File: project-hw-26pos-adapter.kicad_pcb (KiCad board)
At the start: 2 copper layers, 38 x 52 mm, 3 parts, among them J1 SM04B-SRSS-TB(LF)(SN), J2 3220-26-0300-00, U1 Pink Panda v2.1.0

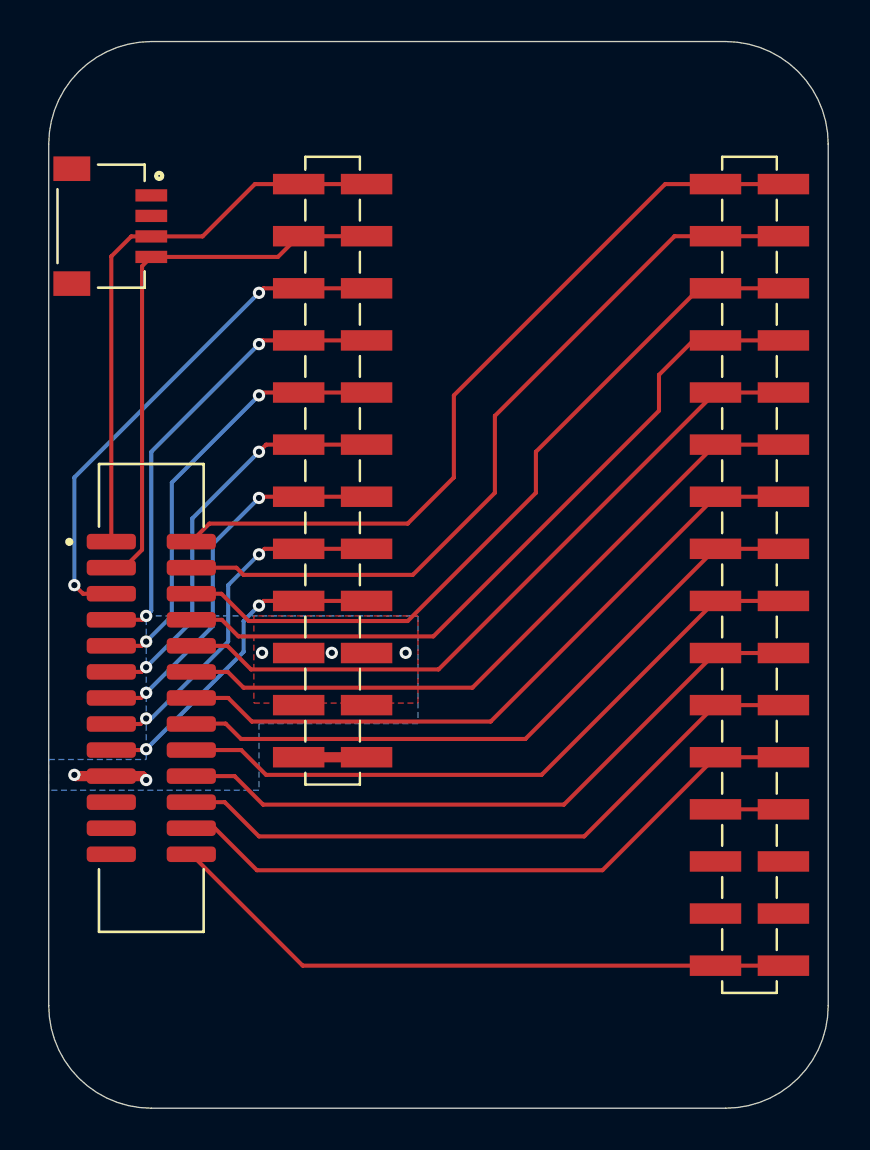
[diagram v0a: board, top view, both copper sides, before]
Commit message: pcb: complete routing
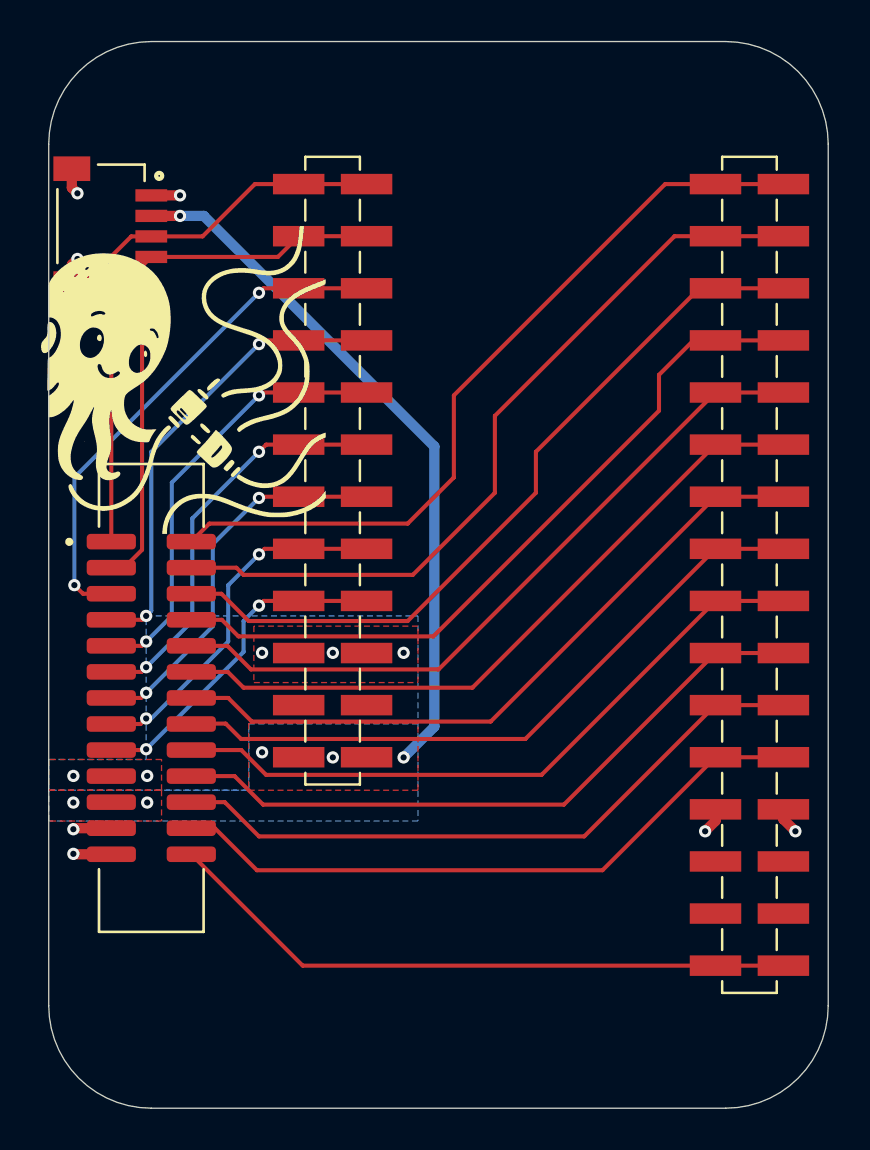
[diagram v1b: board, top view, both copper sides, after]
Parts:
- added G***: LOGO, logos:octopus_15mm, F.Cu at (38.0, 35.5)
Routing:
- net /VDD_OUT: track 3.31 -> 34.2 mm, vias 0 -> 6
- net GND: track 3.31 -> 10.3 mm, vias 0 -> 7
- net /USB: track 3.60 -> 0.00 mm
- added copper zone on B.Cu, net /VDD_OUT
- added copper zone on F.Cu, net /VDD_OUT
- added copper zone on In1.Cu, net GND
- added copper zone on In2.Cu, net GND
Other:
- copper layers 2 -> 4

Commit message: Print 1:1
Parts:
- moved G*** 0.25 mm to (38.2, 35.5)
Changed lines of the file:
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@@
 	(footprint "logos:octopus_15mm"
 		(layer "F.Cu")
-		(at 38 35.5)
+		(at 38.25 35.5)
 		(property "Reference" "G***"
 			(at 0 0 0)

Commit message: pcb: add version on board
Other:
- board text added: "v1.0.0"
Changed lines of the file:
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@@
 		(layer "Edge.Cuts")
+	)
+	(gr_text "v1.0.0"
+		(at 68 68 0)
+		(layer "B.SilkS")
+		(effects
+			(font
+				(face "FreeSans")
+				(size 1.5 1.5)
+				(thickness 0.1)
+			)
+			(justify left bottom mirror)
+		)
+		(render_cache "v1.0.0" 0
+			(polygon
+				(pts
+					(xy 67.398429 67.745) (xy 67.590771 67.745) (xy 67.97875 66.642976) (xy 67.780547 66.642976) (xy 67.485258 67.536905)
+					(xy 67.172749 66.642976) (xy 66.974546 66.642976)
+				)
+			)
+			(polygon
+				(pts
+					(xy 66.412909 66.666423) (xy 66.744103 66.666423) (xy 66.744103 66.525739) (xy 66.668712 66.515289)
+					(xy 66.594039 66.501339) (xy 66.519052 66.480622) (xy 66.463468 66.453932) (xy 66.413026 66.397253)
+					(xy 66.378093 66.327158) (xy 66.352568 66.254492) (xy 66.349528 66.244371) (xy 66.227163 66.244371)
+					(xy 66.227163 67.745) (xy 66.412909 67.745)
+				)
+			)
+			(polygon
+				(pts
+					(xy 65.404675 67.533974) (xy 65.404675 67.745) (xy 65.624127 67.745) (xy 65.624127 67.533974)
+				)
+			)
+			(polygon
+				(pts
+					(xy 64.747572 66.247597) (xy 64.819958 66.261224) (xy 64.88758 66.288643) (xy 64.949651 66.328635)
+					(xy 64.97026 66.345072) (xy 65.023114 66.399087) (xy 65.065788 66.459794) (xy 65.068794 66.464892)
+					(xy 65.10236 66.53556) (xy 65.126789 66.607831) (xy 65.146022 66.683276) (xy 65.149837 66.701308)
+					(xy 65.162637 66.77687) (xy 65.171498 66.857929) (xy 65.176021 66.933362) (xy 65.177529 67.013004)
+					(xy 65.177408 67.03664) (xy 65.174488 67.127627) (xy 65.167676 67.212924) (xy 65.156971 67.292531)
+					(xy 65.142374 67.366448) (xy 65.118653 67.450842) (xy 65.08885 67.526346) (xy 65.052965 67.592958)
+					(xy 65.036943 67.617048) (xy 64.983448 67.679993) (xy 64.921813 67.72895) (xy 64.852037 67.763919)
+					(xy 64.774122 67.7849) (xy 64.688066 67.791894) (xy 64.658696 67.791126) (xy 64.57589 67.779598)
+					(xy 64.501045 67.754237) (xy 64.434159 67.715043) (xy 64.375233 67.662017) (xy 64.324267 67.595157)
+					(xy 64.316536 67.582666) (xy 64.281561 67.515073) (xy 64.252722 67.438911) (xy 64.23002 67.35418)
+					(xy 64.216275 67.280226) (xy 64.206458 67.200788) (xy 64.200567 67.115866) (xy 64.198604 67.02546)
+					(xy 64.198945 67.008607) (xy 64.388381 67.008607) (xy 64.389537 67.085246) (xy 64.394234 67.173767)
+					(xy 64.402546 67.254203) (xy 64.41447 67.326553) (xy 64.43355 67.402699) (xy 64.462386 67.476821)
+					(xy 64.492912 67.528118) (xy 64.549616 67.585163) (xy 64.619419 67.618329) (xy 64.692463 67.627763)
+					(xy 64.777532 67.612799) (xy 64.848182 67.567907) (xy 64.894321 67.510445) (xy 64.931232 67.433829)
+					(xy 64.95286 67.363797) (xy 64.969297 67.282991) (xy 64.980543 67.191411) (xy 64.986599 67.089057)
+					(xy 64.987752 67.014836) (xy 64.98746 66.977532) (xy 64.98307 66.872726) (xy 64.973412 66.778579)
+					(xy 64.958486 66.69509) (xy 64.930391 66.60035) (xy 64.89293 66.524559) (xy 64.846104 66.467715)
+					(xy 64.774402 66.423306) (xy 64.688066 66.408503) (xy 64.651776 66.410847) (xy 64.571294 66.437219)
+					(xy 64.505445 66.492892) (xy 64.463302 66.558529) (xy 64.430524 66.642919) (xy 64.412086 66.718518)
+					(xy 64.398916 66.804665) (xy 64.391014 66.901362) (xy 64.388381 67.008607) (xy 64.198945 67.008607)
+					(xy 64.200516 66.930875) (xy 64.206252 66.842392) (xy 64.215811 66.760012) (xy 64.229195 66.683734)
+					(xy 64.256441 66.580758) (xy 64.29229 66.491513) (xy 64.336743 66.415997) (xy 64.3898 66.354212)
+					(xy 64.451461 66.306157) (xy 64.521726 66.271832) (xy 64.600594 66.251236) (xy 64.688066 66.244371)
+				)
+			)
+			(polygon
+				(pts
+					(xy 63.713538 67.533974) (xy 63.713538 67.745) (xy 63.93299 67.745) (xy 63.93299 67.533974)
+				)
+			)
+			(polygon
+				(pts
+					(xy 63.056435 66.247597) (xy 63.12882 66.261224) (xy 63.196442 66.288643) (xy 63.258513 66.328635)
+					(xy 63.279123 66.345072) (xy 63.331977 66.399087) (xy 63.374651 66.459794) (xy 63.377657 66.464892)
+					(xy 63.411222 66.53556) (xy 63.435651 66.607831) (xy 63.454884 66.683276) (xy 63.4587 66.701308)
+					(xy 63.4715 66.77687) (xy 63.480361 66.857929) (xy 63.484884 66.933362) (xy 63.486392 67.013004)
+					(xy 63.48627 67.03664) (xy 63.483351 67.127627) (xy 63.476538 67.212924) (xy 63.465834 67.292531)
+					(xy 63.451236 67.366448) (xy 63.427516 67.450842) (xy 63.397713 67.526346) (xy 63.361828 67.592958)
+					(xy 63.345805 67.617048) (xy 63.29231 67.679993) (xy 63.230675 67.72895) (xy 63.1609 67.763919)
+					(xy 63.082985 67.7849) (xy 62.996929 67.791894) (xy 62.967558 67.791126) (xy 62.884753 67.779598)
+					(xy 62.809907 67.754237) (xy 62.743021 67.715043) (xy 62.684095 67.662017) (xy 62.633129 67.595157)
+					(xy 62.625398 67.582666) (xy 62.590424 67.515073) (xy 62.561585 67.438911) (xy 62.538882 67.35418)
+					(xy 62.525138 67.280226) (xy 62.51532 67.200788) (xy 62.50943 67.115866) (xy 62.507466 67.02546)
+					(xy 62.507807 67.008607) (xy 62.697243 67.008607) (xy 62.698399 67.085246) (xy 62.703097 67.173767)
+					(xy 62.711408 67.254203) (xy 62.723333 67.326553) (xy 62.742412 67.402699) (xy 62.771249 67.476821)
+					(xy 62.801774 67.528118) (xy 62.858478 67.585163) (xy 62.928282 67.618329) (xy 63.001325 67.627763)
+					(xy 63.086394 67.612799) (xy 63.157045 67.567907) (xy 63.203184 67.510445) (xy 63.240095 67.433829)
+					(xy 63.261722 67.363797) (xy 63.278159 67.282991) (xy 63.289406 67.191411) (xy 63.295462 67.089057)
+					(xy 63.296615 67.014836) (xy 63.296322 66.977532) (xy 63.291932 66.872726) (xy 63.282275 66.778579)
+					(xy 63.267349 66.69509) (xy 63.239253 66.60035) (xy 63.201792 66.524559) (xy 63.154967 66.467715)
+					(xy 63.083264 66.423306) (xy 62.996929 66.408503) (xy 62.960639 66.410847) (xy 62.880157 66.437219)
+					(xy 62.814308 66.492892) (xy 62.772165 66.558529) (xy 62.739386 66.642919) (xy 62.720949 66.718518)
+					(xy 62.707779 66.804665) (xy 62.699877 66.901362) (xy 62.697243 67.008607) (xy 62.507807 67.008607)
+					(xy 62.509378 66.930875) (xy 62.515114 66.842392) (xy 62.524674 66.760012) (xy 62.538058 66.683734)
+					(xy 62.565303 66.580758) (xy 62.601153 66.491513) (xy 62.645606 66.415997) (xy 62.698663 66.354212)
+					(xy 62.760324 66.306157) (xy 62.830588 66.271832) (xy 62.909457 66.251236) (xy 62.996929 66.244371)
+				)
+			)
+		)
 	)
 	(segment

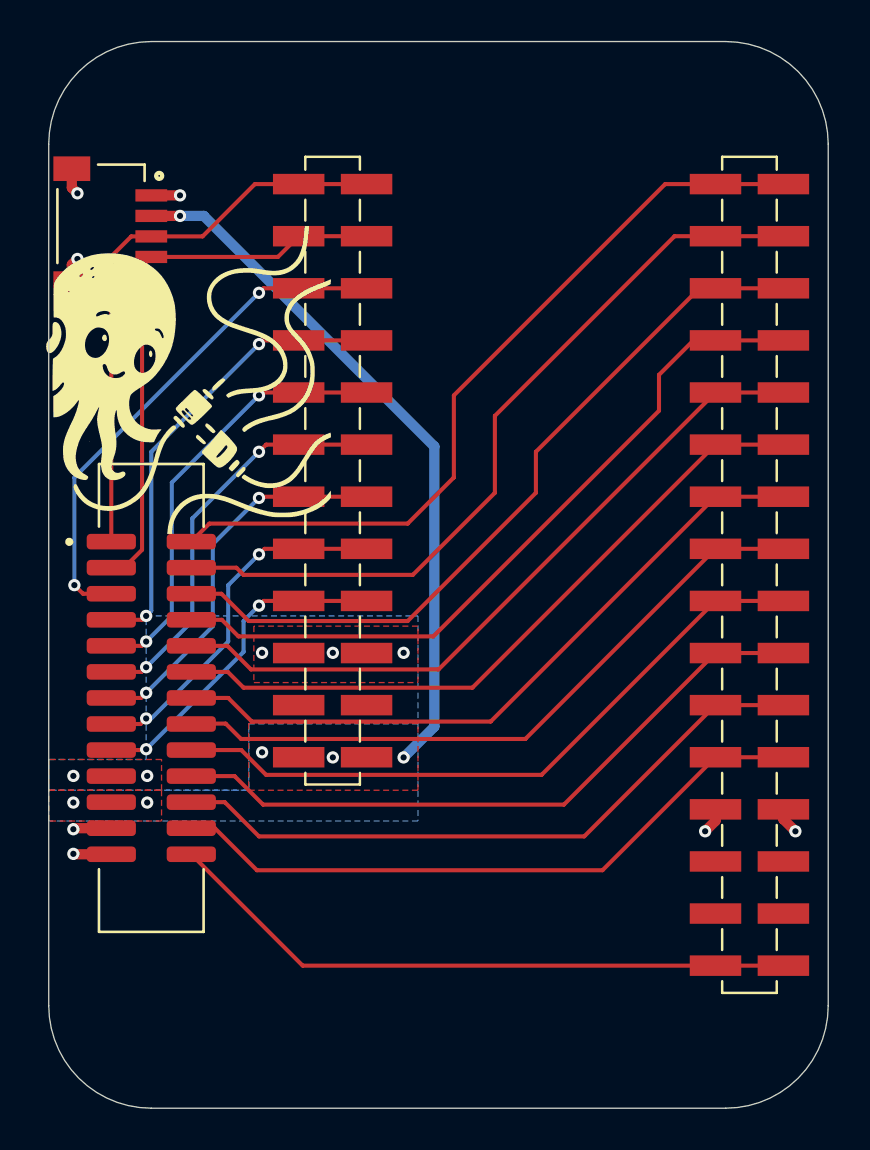
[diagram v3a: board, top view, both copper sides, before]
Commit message: Add series resistors
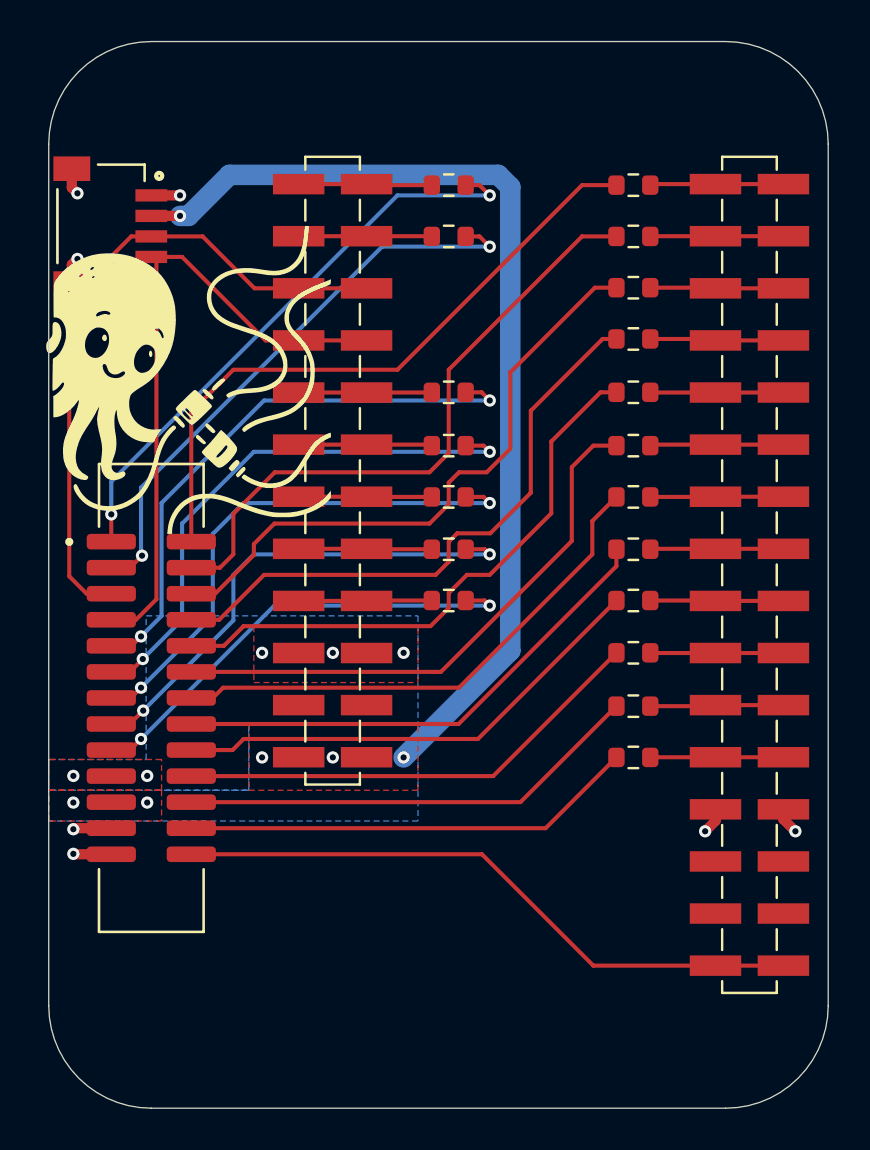
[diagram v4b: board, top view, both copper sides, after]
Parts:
- added R1: R_Small, Resistor_SMD:R_0603_1608Metric, F.Cu at (51.5, 26.0)
- added R10: R_Small, Resistor_SMD:R_0603_1608Metric, F.Cu at (60.5, 31.0)
- added R11: R_Small, Resistor_SMD:R_0603_1608Metric, F.Cu at (60.5, 33.5)
- added R12: R_Small, Resistor_SMD:R_0603_1608Metric, F.Cu at (60.5, 36.1)
- added R13: R_Small, Resistor_SMD:R_0603_1608Metric, F.Cu at (60.5, 38.7)
- added R14: R_Small, Resistor_SMD:R_0603_1608Metric, F.Cu at (60.5, 41.2)
- added R15: R_Small, Resistor_SMD:R_0603_1608Metric, F.Cu at (60.5, 43.8)
- added R16: R_Small, Resistor_SMD:R_0603_1608Metric, F.Cu at (60.5, 46.2)
- added R17: R_Small, Resistor_SMD:R_0603_1608Metric, F.Cu at (60.5, 48.8)
- added R18: R_Small, Resistor_SMD:R_0603_1608Metric, F.Cu at (60.5, 51.4)
- added R19: R_Small, Resistor_SMD:R_0603_1608Metric, F.Cu at (60.5, 53.9)
- added R2: R_Small, Resistor_SMD:R_0603_1608Metric, F.Cu at (51.5, 28.5)
- added R3: R_Small, Resistor_SMD:R_0603_1608Metric, F.Cu at (51.5, 36.1)
- added R4: R_Small, Resistor_SMD:R_0603_1608Metric, F.Cu at (51.5, 38.7)
- added R5: R_Small, Resistor_SMD:R_0603_1608Metric, F.Cu at (51.5, 41.2)
- added R6: R_Small, Resistor_SMD:R_0603_1608Metric, F.Cu at (51.5, 43.8)
- added R7: R_Small, Resistor_SMD:R_0603_1608Metric, F.Cu at (51.5, 46.2)
- added R8: R_Small, Resistor_SMD:R_0603_1608Metric, F.Cu at (60.5, 26.0)
- added R9: R_Small, Resistor_SMD:R_0603_1608Metric, F.Cu at (60.5, 28.5)
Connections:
- J1 pad 3: /P0.27 -> /P0.04
- J1 pad 4: /P0.05 -> /P0.26
- U1 pad 1: /P0.27 -> Net-(U1-P0.27)
- U1 pad 13: /P0.20 -> Net-(U1-P0.20)
- U1 pad 14: /P0.21 -> Net-(U1-P0.21)
- U1 pad 15: /P0.15 -> Net-(U1-P0.15)
- U1 pad 16: /P0.19 -> Net-(U1-P0.19)
- U1 pad 17: /P1.00 -> Net-(U1-P1.00)
- U1 pad 18: /P0.24 -> Net-(U1-P0.24)
- U1 pad 19: /P0.22 -> Net-(U1-P0.22)
- U1 pad 2: /P0.05 -> Net-(U1-P0.05)
- U1 pad 20: /P0.23 -> Net-(U1-P0.23)
- U1 pad 21: /P0.17 -> Net-(U1-P0.17)
- U1 pad 22: /P0.13 -> Net-(U1-P0.13)
- U1 pad 23: /P0.09 -> Net-(U1-P0.09)
- U1 pad 24: /P0.10 -> Net-(U1-P0.10)
- U1 pad 5: /P0.07 -> Net-(U1-P0.07)
- U1 pad 6: /P0.06 -> Net-(U1-P0.06)
- U1 pad 7: /P0.29 -> Net-(U1-P0.29)
- U1 pad 8: /P0.28 -> Net-(U1-P0.28)
- U1 pad 9: /P0.30 -> Net-(U1-P0.30)
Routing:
- net /VDD_OUT: track 34.2 -> 48.5 mm
- net /P0.10: track 32.0 -> 22.2 mm
- net /P0.09: track 32.2 -> 22.7 mm
- net /P0.13: track 32.5 -> 23.2 mm
- net /P0.17: track 32.9 -> 23.7 mm
- net /P0.26: track 22.6 -> 31.6 mm, vias 2 -> 0
- net /P0.23: track 33.0 -> 24.7 mm
- net /P0.22: track 33.9 -> 25.7 mm
- net /P0.04: track 25.3 -> 32.7 mm, vias 2 -> 0
- net /P0.15: track 37.3 -> 30.0 mm
- net /P0.29: track 18.9 -> 26.0 mm
- net /P0.21: track 38.0 -> 31.0 mm
- net /P0.06: track 20.0 -> 26.9 mm
- net /P0.19: track 36.2 -> 29.3 mm
- net /P0.28: track 17.6 -> 24.5 mm
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
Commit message: pcb: update version on silkscreen
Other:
- board text added: "v1.0.0-2-g7777ac5"
- board text removed: "v1.0.0"
